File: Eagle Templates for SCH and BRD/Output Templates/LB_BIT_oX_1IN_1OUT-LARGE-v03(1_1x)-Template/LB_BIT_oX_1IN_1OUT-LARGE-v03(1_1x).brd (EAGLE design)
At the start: 21.4 x 24.8 mm, 17 parts, among them U1 LV321SOT23-5, U2 LV321SOT23-5

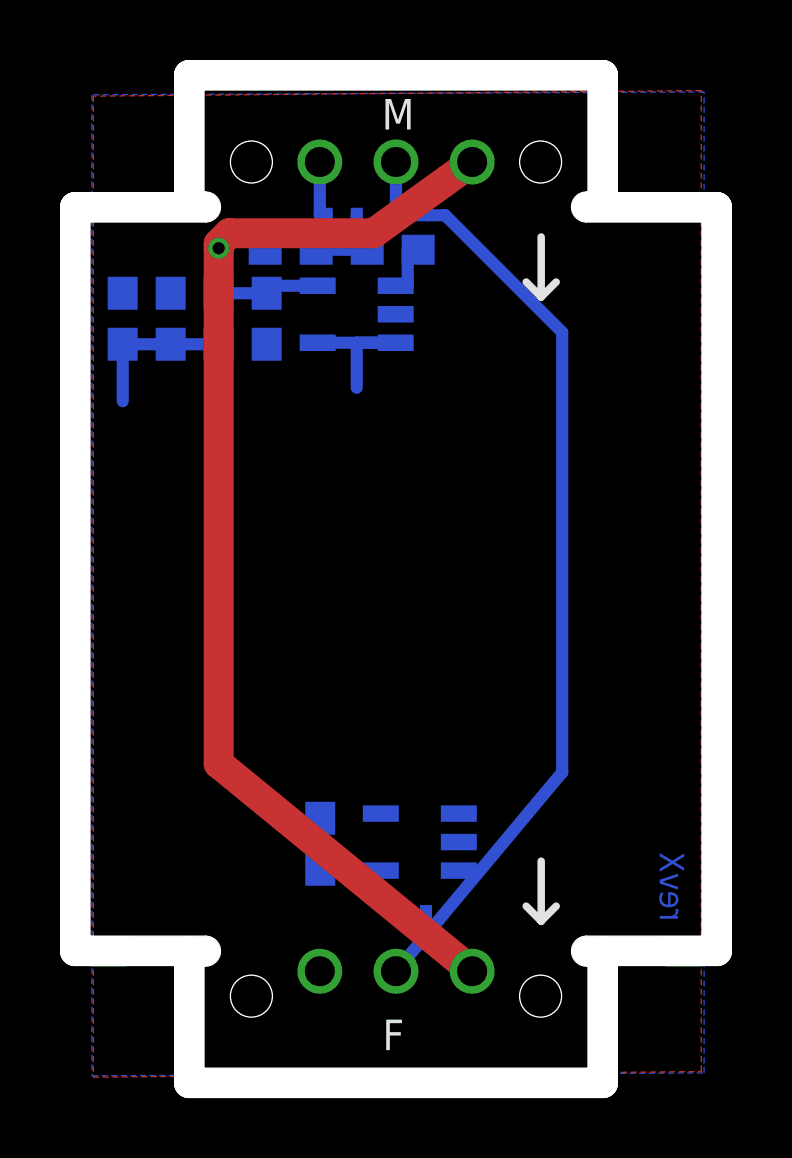
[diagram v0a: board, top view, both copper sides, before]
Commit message: added bitlab logo and made minor changes to board templates. Updated littlebits library.
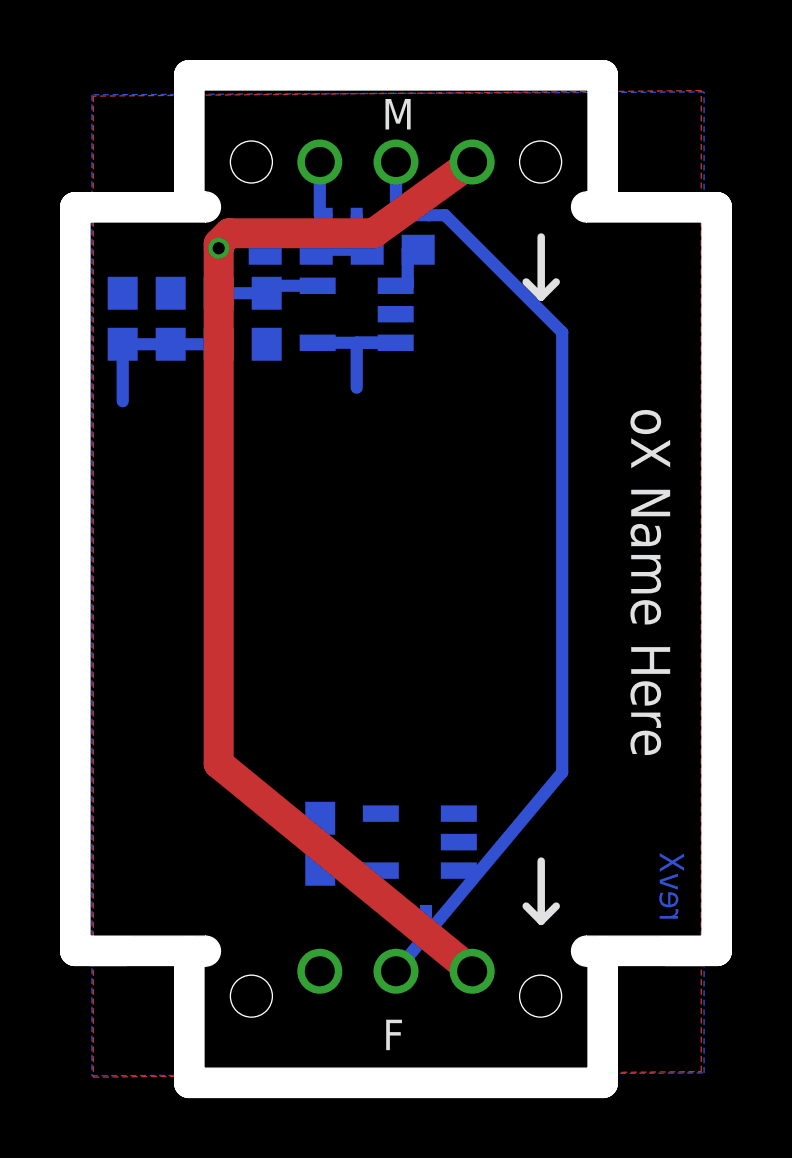
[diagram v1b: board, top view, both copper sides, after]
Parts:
- added U$5: (no value), LITTLEBITS:BITLAB-LOGO
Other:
- board text added: "oX Name Here"
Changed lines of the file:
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@@
 <layer number="111" name="LB_TEXT" color="13" fill="1" visible="yes" active="yes"/>
 <layer number="112" name="tSilk" color="7" fill="1" visible="yes" active="yes"/>
+<layer number="113" name="ReferenceLS" color="7" fill="1" visible="no" active="yes"/>
 <layer number="116" name="Patch_BOT" color="9" fill="4" visible="yes" active="yes"/>
+<layer number="118" name="Rect_Pads" color="7" fill="1" visible="no" active="yes"/>
 <layer number="121" name="_tsilk" color="7" fill="1" visible="yes" active="yes"/>
 <layer number="122" name="_bsilk" color="7" fill="1" visible="yes" active="yes"/>
@@
 <wire x1="2.51" y1="28.915" x2="4.21" y2="28.915" width="1" layer="46"/>
 <text x="22" y="5.1" size="0.8128" layer="16" font="vector" ratio="12" rot="MR90">revX</text>
+<text x="21.7" y="16.4" size="1.3" layer="21" font="vector" rot="SR270" align="center">oX Name Here</text>
 </plain>
 <attributes>
@@
 <element name="U$4" library="ohw-logo" package="OSHW_FILLX150_NOTEXT" value="" x="19" y="23.5" rot="MR90"/>
 <element name="U$2" library="LITTLEBITS" package="FABDWG01-OHW" value="FRAME-LETTER" x="0" y="0"/>
+<element name="U$5" library="LITTLEBITS" package="BITLAB-LOGO" value="" x="19.7" y="20.8" rot="R270"/>
 </elements>
 <signals>

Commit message: Updated templates
- Added ferrite beads
- Moved text and annotations off of Nets layer
- Minor layout changes
- Removed I/O/W prefix from reference designators
- Removed output stage components from output bits
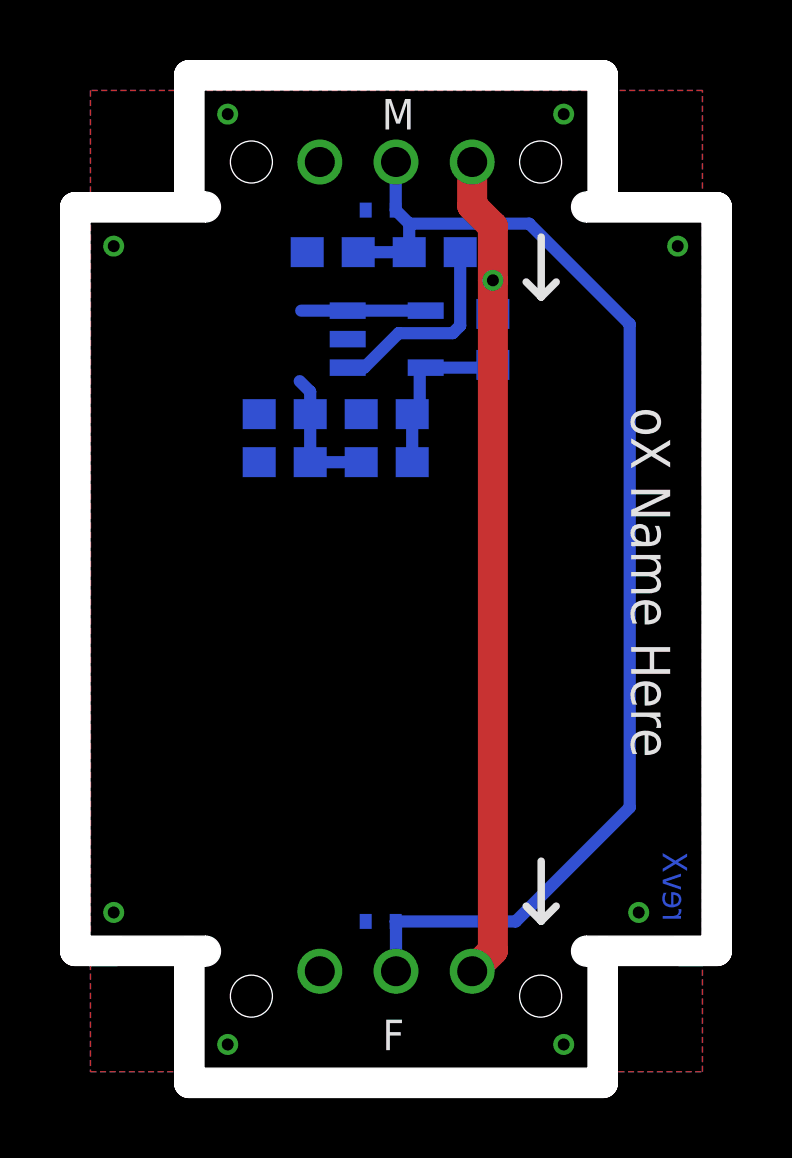
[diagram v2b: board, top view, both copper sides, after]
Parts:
- removed I?C1: 0.1uF, LITTLEBITS:CAP-0603
- removed I?C2: 10uF, LITTLEBITS:CAP-0603
- removed I?C3: 1.0uF, LITTLEBITS:CAP-0603
- removed I?R1: 1meg, LITTLEBITS:RES-0603
- removed I?R2: 10K, LITTLEBITS:RES-0603
- removed I?R3, I?R4: 3K3, LITTLEBITS:RES-0603
- removed I?TVS1, I?TVS2: ESD9B5.0ST5G, LITTLEBITS:SOD-923
- removed U2: LV321SOT23-5, LITTLEBITS:SOT23-5
- added C1: 0.1uF, LITTLEBITS:CAP-0603
- added C2: 10uF, LITTLEBITS:CAP-0603
- added FB1: FERRITE-BEAD0603, LITTLEBITS:R0603
- added R1: 1meg, LITTLEBITS:RES-0603
- added R2: 10K, LITTLEBITS:RES-0603
- added R3, R4: 3K3, LITTLEBITS:RES-0603
- added TVS1, TVS2: ESD9B5.0ST5G, LITTLEBITS:SOD-923
- U$1: value OSHWCREDIT -> OSHW-LOGOL; device LITTLEBITS:OSHWCREDIT -> LITTLEBITS131206:OSHW-LOGO-L
- U$2: value FRAME-LETTER -> OSHWCREDIT; device LITTLEBITS:FABDWG01-OHW -> LITTLEBITS:OSHWCREDIT
- U$3: value OSHW-LOGOL -> FRAME-LETTER; device LITTLEBITS131206:OSHW-LOGO-L -> LITTLEBITS:FABDWG01-OHW
- moved U$2 112.4 mm to (-92.2, -64.3)
- moved U$3 73.1 mm to (0.00, 0.00)
- moved U$1 55.6 mm to (-37.5, -68.2)
- moved U1 1.30 mm to (12.9, 24.5), turned to 90 degrees
- renumbered I?BSF to BSF1, I?BSM to BSM1
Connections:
- removed net N$3: U2.1
- removed net SIG_IN: BSF1.SIG, BSM1.SIG1, I?R1.2, I?R2.2, I?TVS1.2
- removed net SIG_OUT: I?TVS2.2, U2.3, U2.4
- new net LB_VCC: BSF1.VCC, BSM1.VCC1, FB1.2
- new net SIG: BSF1.SIG, BSM1.SIG1, R1.2, R2.2, TVS1.2, TVS2.2
- net GND: now also C1.2, C2.2, R1.1, R4.1, TVS1.1, TVS2.1; no longer I?C1.2, I?C2.2, I?C3.1, I?R1.1, I?R4.1, I?TVS1.1, I?TVS2.1, U2.2
- net N$4: now also R2.1; no longer I?R2.1
- net VCC: now also C1.1, FB1.1, R3.2; no longer BSF1.VCC, BSM1.VCC1, I?C1.1, I?C3.2, I?R3.2, U2.5
- net VREF: now also C2.1, R3.1, R4.2; no longer I?C2.1, I?R3.1, I?R4.2
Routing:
- net SIG: track 0.00 -> 40.8 mm
- net VCC: track 44.6 -> 5.91 mm, vias 1 -> 0
- net SIG_IN: track 35.4 -> 0.00 mm
- net LB_VCC: track 0.00 -> 28.7 mm, vias 0 -> 1
- net N$4: track 1.95 -> 6.78 mm
- net GND: track 2.00 -> 0.00 mm, vias 0 -> 8
- net N$2: track 5.40 -> 4.15 mm
- net VREF: track 5.10 -> 4.54 mm
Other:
- outline, holes or cut-outs redrawn
